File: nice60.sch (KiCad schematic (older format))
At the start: 140 parts, among them J1 USB_C_Receptacle_USB2.0, J2 Conn_01x04_Female, J3 Conn_01x02_Female, SW1 SW_Push, U1 ProMicro, U2 USBLC6-2SC6

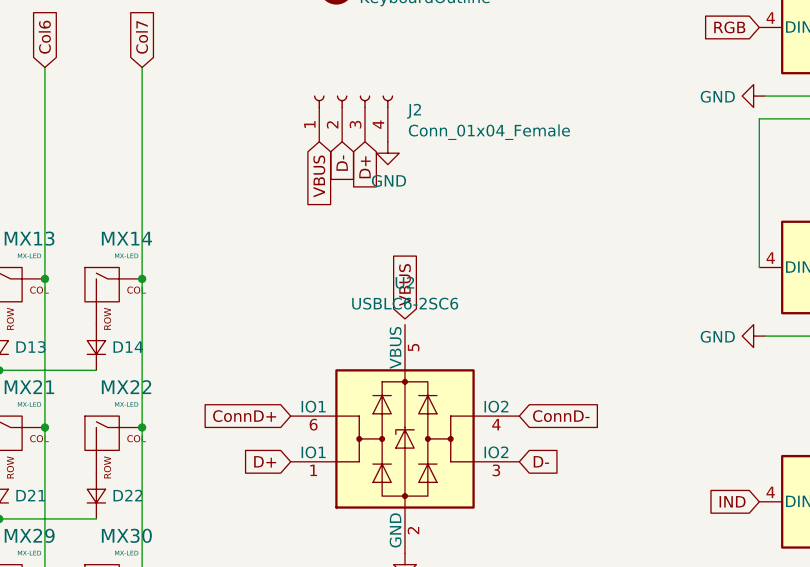
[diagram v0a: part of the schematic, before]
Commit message: Fix VBUS connection to ESD protection
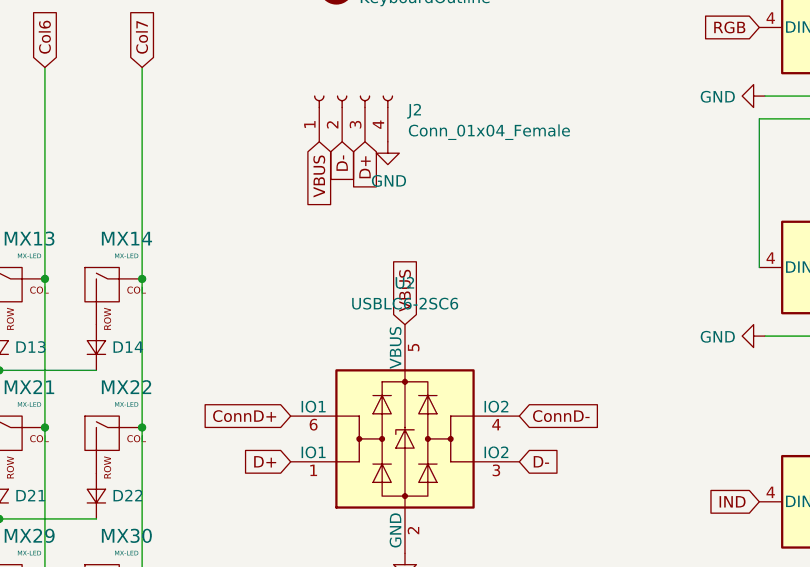
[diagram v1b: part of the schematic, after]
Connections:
- net VBUS: now also U2.5 (VBUS)
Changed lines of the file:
@@
 	1    0    0    -1
 $EndComp
-Text GLabel 5650 2375 1    50   Input ~ 0
+Text GLabel 5650 2400 1    50   Input ~ 0
 VBUS
 Text GLabel 6150 3000 2    50   Input ~ 0
